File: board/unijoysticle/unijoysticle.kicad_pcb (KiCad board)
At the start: 2 copper layers, 55.6 x 40.6 mm, 13 parts, among them IC1 7405, IC2 7405, J1 DB9_Female, J2 DB9_Female, J3 Barrel_Jack, SW1 SW_Push

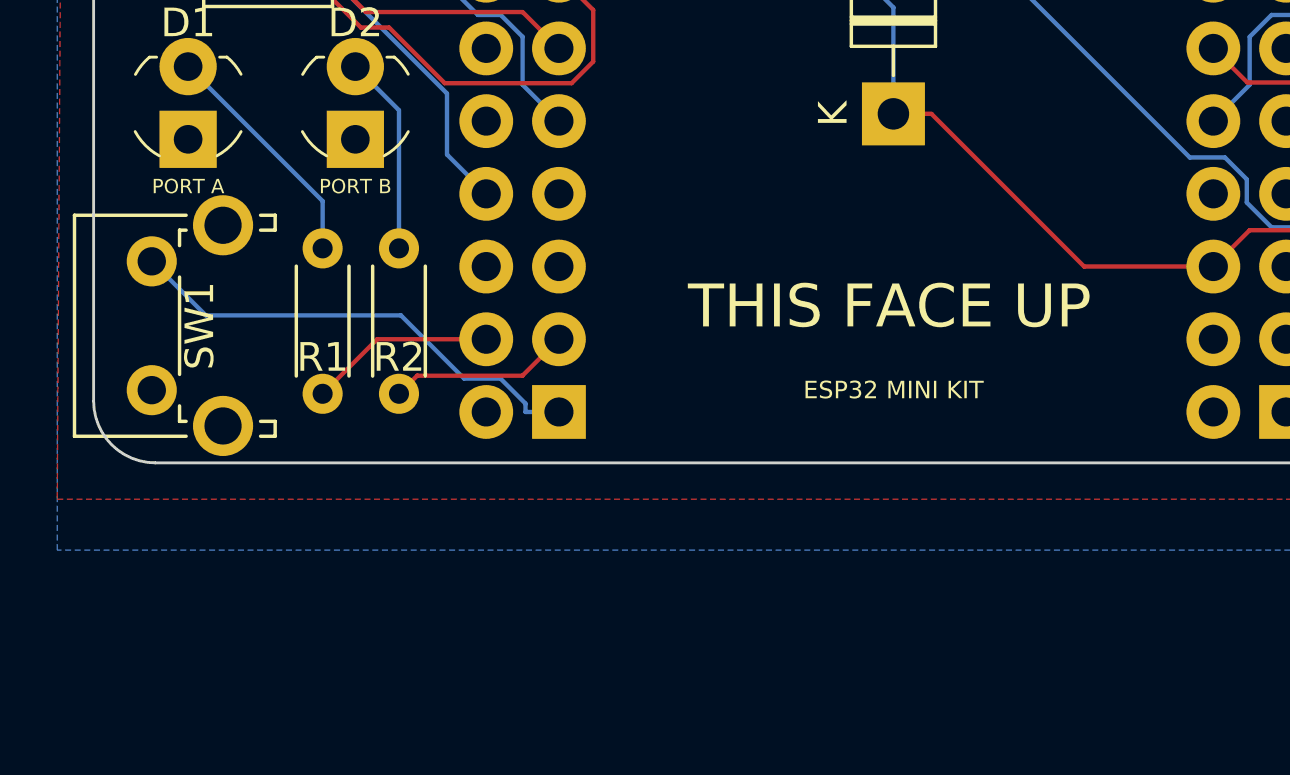
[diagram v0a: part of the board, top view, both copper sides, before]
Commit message: board: renamed 'Parts' -> 'Unijoysticle'
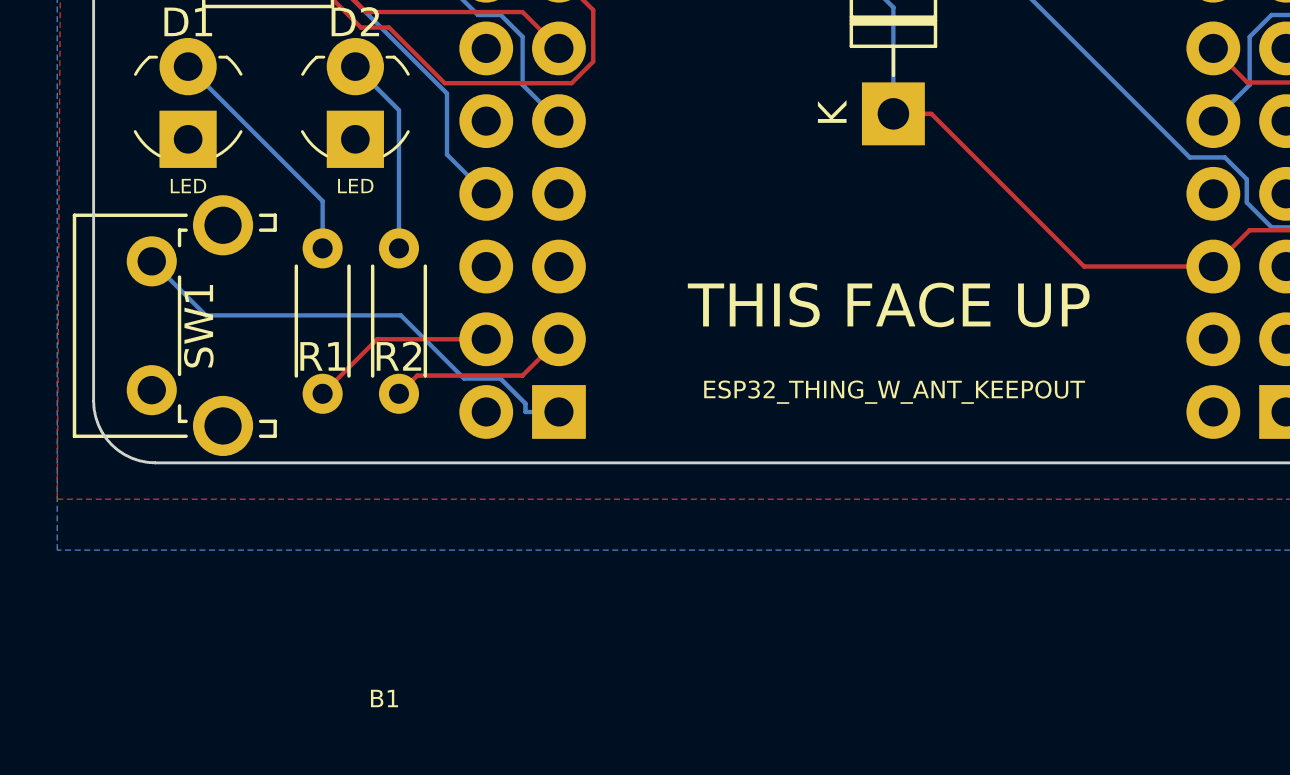
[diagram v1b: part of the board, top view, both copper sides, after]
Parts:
- B1: renamed from ?; value ESP32 MINI KIT -> ESP32_THING_W_ANT_KEEPOUT
- D1: value PORT A -> LED
- D2: value PORT B -> LED
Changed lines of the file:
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@@
-(kicad_pcb (version 20171130) (host pcbnew "(5.0.2-5-10.14)")
+(kicad_pcb (version 20171130) (host pcbnew "(5.1.0-0)")
   (general
     (thickness 1.6002)
@@
     (zone_45_only no)
     (trace_min 0.1524)
-    (segment_width 0.2)
-    (edge_width 0.1)
     (via_size 0.6858)
     (via_drill 0.3302)
@@
     (uvia_min_size 0.2)
     (uvia_min_drill 0.1)
+    (edge_width 0.1)
+    (segment_width 0.2)
     (pcb_text_width 0.3)
     (pcb_text_size 1.5 1.5)
@@
       (effects (font (size 1 1) (thickness 0.15)))
     )
-    (fp_text value "PORT A" (at -4.191 0 180) (layer F.SilkS)
+    (fp_text value LED (at -4.191 0 180) (layer F.SilkS)
       (effects (font (size 0.5 0.5) (thickness 0.1)))
     )
@@
     (descr "MH-ET LIVE MiniKit for ESP32")
     (tags ESP32)
-    (fp_text reference "" (at -2.286 1.143) (layer F.SilkS)
+    (fp_text reference B1 (at -2.286 1.143) (layer F.SilkS)
       (effects (font (size 0.6096 0.6096) (thickness 0.127)))
     )
-    (fp_text value "ESP32 MINI KIT" (at 15.494 -9.652 180) (layer F.SilkS)
+    (fp_text value ESP32_THING_W_ANT_KEEPOUT (at 15.494 -9.652 180) (layer F.SilkS)
       (effects (font (size 0.6096 0.6096) (thickness 0.127)))
     )
@@
       (effects (font (size 1 1) (thickness 0.15)))
     )
-    (fp_text value "PORT B" (at -4.191 0) (layer F.SilkS)
+    (fp_text value LED (at -4.191 0) (layer F.SilkS)
       (effects (font (size 0.5 0.5) (thickness 0.1)))
     )

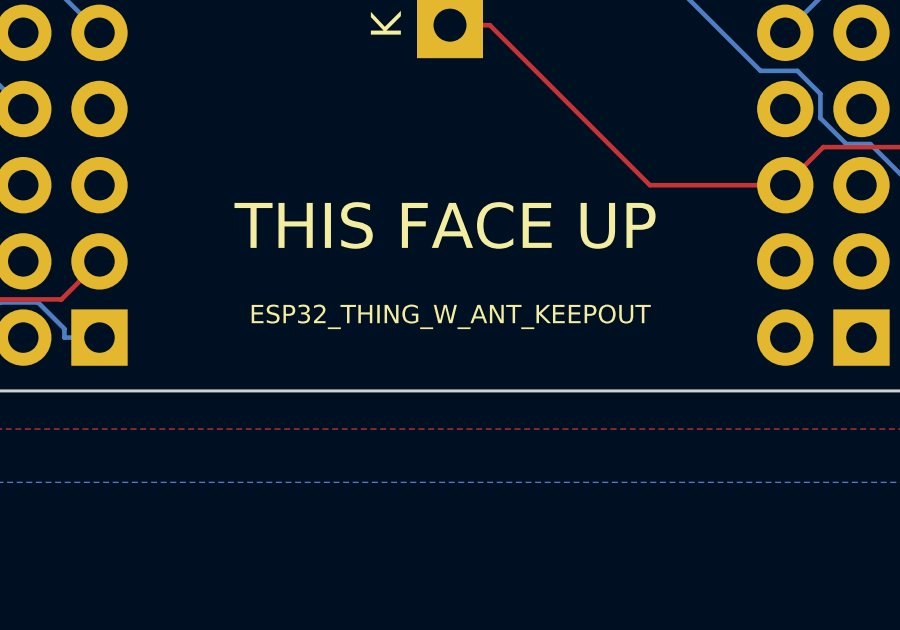
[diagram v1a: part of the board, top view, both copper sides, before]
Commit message: firmware: uni_gpio
schematic: borders around components
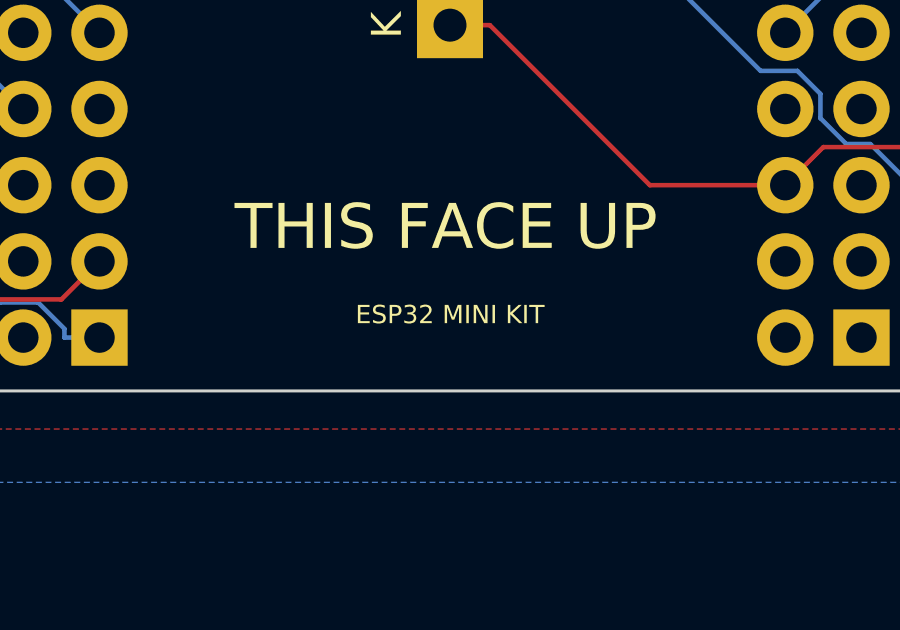
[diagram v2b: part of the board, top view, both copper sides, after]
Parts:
- B1: value ESP32_THING_W_ANT_KEEPOUT -> ESP32 MINI KIT
- R1, R2: value R -> 100
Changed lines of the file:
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@@
   (general
     (thickness 1.6002)
-    (drawings 13)
+    (drawings 12)
     (tracks 169)
     (zones 0)
@@
   )
   (page A4)
+  (title_block
+    (title Unijoysticle)
+    (date 2019-03-13)
+    (rev v0.0.1)
+  )
   (layers
     (0 F.Cu signal)
@@
       (effects (font (size 0.6096 0.6096) (thickness 0.127)))
     )
-    (fp_text value ESP32_THING_W_ANT_KEEPOUT (at 15.494 -9.652 180) (layer F.SilkS)
+    (fp_text value "ESP32 MINI KIT" (at 15.494 -9.652 180) (layer F.SilkS)
       (effects (font (size 0.6096 0.6096) (thickness 0.127)))
     )
@@
       (effects (font (size 1 1) (thickness 0.15)))
     )
-    (fp_text value R (at -1.905 0 180) (layer F.Fab)
+    (fp_text value 100 (at -1.905 0 180) (layer F.Fab)
       (effects (font (size 1 1) (thickness 0.15)))
     )
@@
       (effects (font (size 1 1) (thickness 0.15)))
     )
-    (fp_text value R (at -1.905 0 180) (layer F.Fab)
+    (fp_text value 100 (at -1.905 0 180) (layer F.Fab)
       (effects (font (size 1 1) (thickness 0.15)))
     )
@@
     (effects (font (size 1.5 1.5) (thickness 0.3)) (justify mirror))
   )
-  (dimension 20.955 (width 0.3) (layer Dwgs.User)
-    (gr_text "20.955 mm" (at 142.3035 43.493) (layer Dwgs.User)
-      (effects (font (size 1.5 1.5) (thickness 0.3)))
-    )
-    (feature1 (pts (xy 131.826 79.121) (xy 131.826 45.006579)))
-    (feature2 (pts (xy 152.781 79.121) (xy 152.781 45.006579)))
-    (crossbar (pts (xy 152.781 45.593) (xy 131.826 45.593)))
-    (arrow1a (pts (xy 131.826 45.593) (xy 132.952504 45.006579)))
-    (arrow1b (pts (xy 131.826 45.593) (xy 132.952504 46.179421)))
-    (arrow2a (pts (xy 152.781 45.593) (xy 151.654496 45.006579)))
-    (arrow2b (pts (xy 152.781 45.593) (xy 151.654496 46.179421)))
-  )
   (gr_line (start 116.967 115.57) (end 168.275 115.57) (layer Edge.Cuts) (width 0.1))

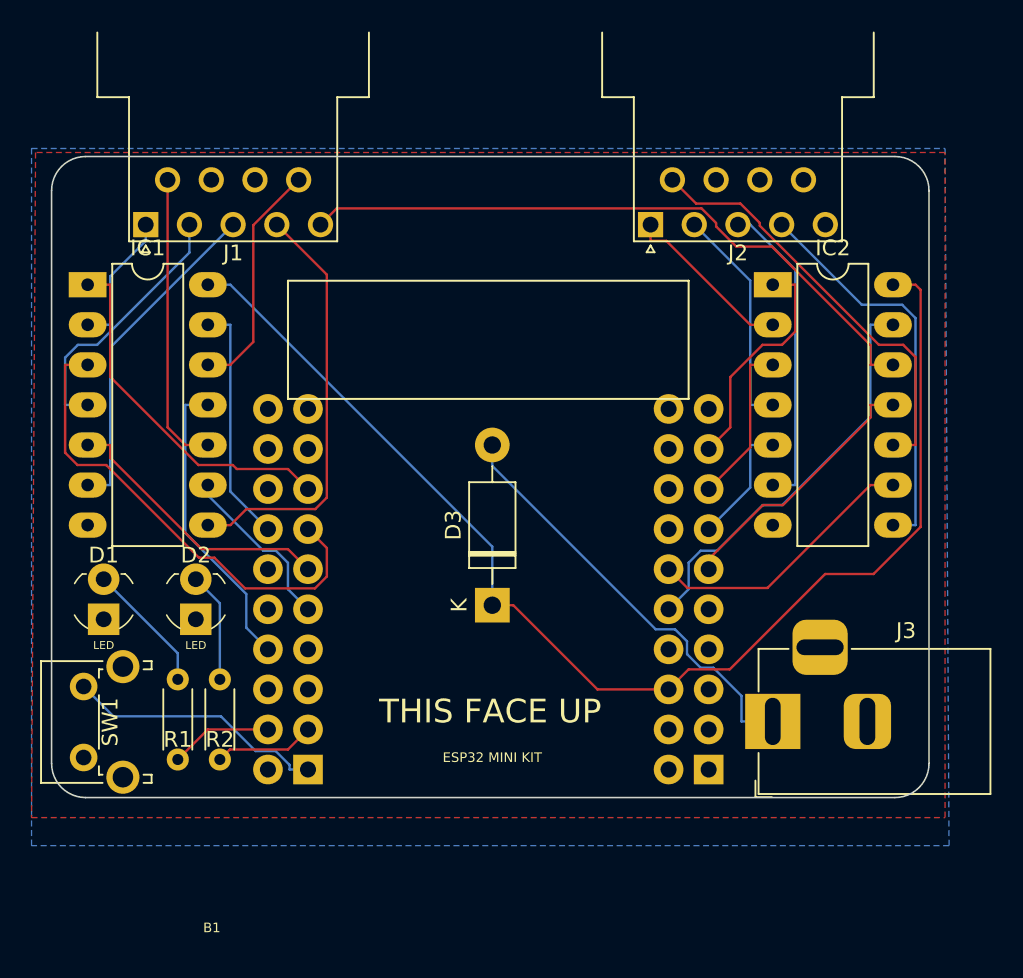
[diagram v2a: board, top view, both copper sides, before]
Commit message: firmware: support for new mappings (v2)
board: board slightly bigger, diode smaller, resistrors larger
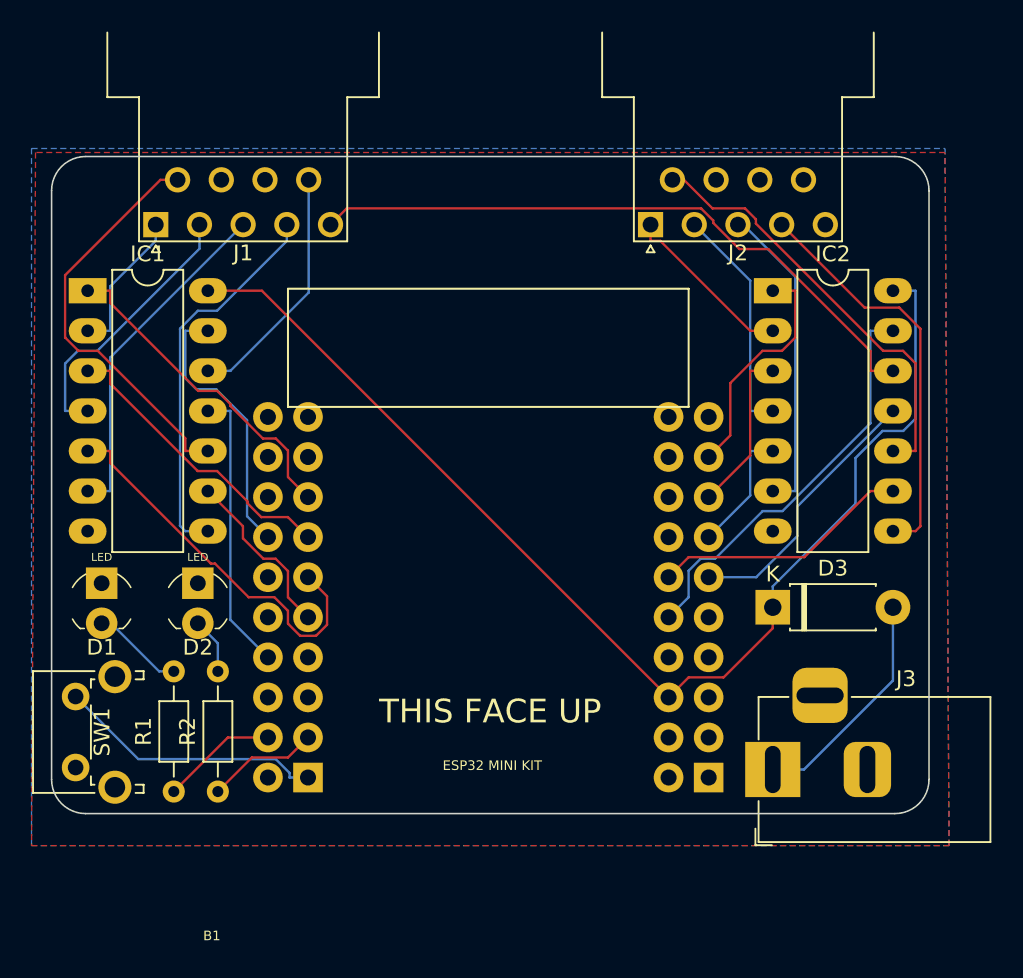
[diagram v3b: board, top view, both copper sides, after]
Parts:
- D3: footprint Diode_THT:D_DO-41_SOD81_P10.16mm_Horizontal -> Diode_THT:D_DO-41_SOD81_P7.62mm_Horizontal
- R1, R2: footprint Resistor_THT:R_Axial_DIN0204_L3.6mm_D1.6mm_P5.08mm_Horizontal -> Resistor_THT:R_Axial_DIN0204_L3.6mm_D1.6mm_P7.62mm_Horizontal
- moved D3 17.8 mm to (160.5, 103.5), turned to 0 degrees
- moved J3 3.05 mm to (160.5, 113.8)
- moved D1 2.80 mm to (118.0, 104.5), turned to 270 degrees
- moved D2 2.80 mm to (124.1, 104.5), turned to 270 degrees
- moved R1 2.05 mm to (122.6, 115.2)
- moved R2 2.04 mm to (125.3, 115.2)
- moved SW1 0.81 mm to (116.3, 113.7)
- moved J1 0.64 mm to (121.4, 79.2)
- moved B1 0.51 mm to (127.3, 123.2)
- moved IC1 0.38 mm to (117.1, 83.4)
- moved IC2 0.38 mm to (160.5, 83.4)
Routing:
- net Net-(D3-Pad2): track 27.2 -> 14.6 mm
- net GPIO_J1DOWN: track 31.0 -> 18.9 mm
- net J1FIRE: track 18.7 -> 26.1 mm
- net GPIO_J1LEFT: track 17.7 -> 24.8 mm
- net VDD: track 79.2 -> 75.6 mm
- net Net-(D2-Pad2): track 6.98 -> 3.57 mm
- net Net-(D1-Pad2): track 8.30 -> 5.83 mm
- net J1RIGHT: track 26.9 -> 24.5 mm
- net GPIO_J1POTX: track 15.4 -> 17.4 mm
- net GPIO_J1UP: track 22.8 -> 20.9 mm
- net GPIO_J1FIRE: track 19.1 -> 18.0 mm
- net GPIO_J2RIGHT: track 17.4 -> 16.5 mm
- net GPIO_J1LED: track 6.50 -> 7.39 mm
- net GPIO_J2LED: track 6.38 -> 7.14 mm
- net J1DOWN: track 16.8 -> 17.5 mm
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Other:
- board size 55.6 x 40.6 mm -> 55.6 x 41.7 mm
- board text added: "Unijoysticle 2 v0.0.2 http://retro.moe"
- board text removed: "Unijoysticle 2 v0.0.1 http://retro.moe"

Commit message: firmware: using GPIOS correctly.
new GPIOS for a some lines so that it doesn't crash
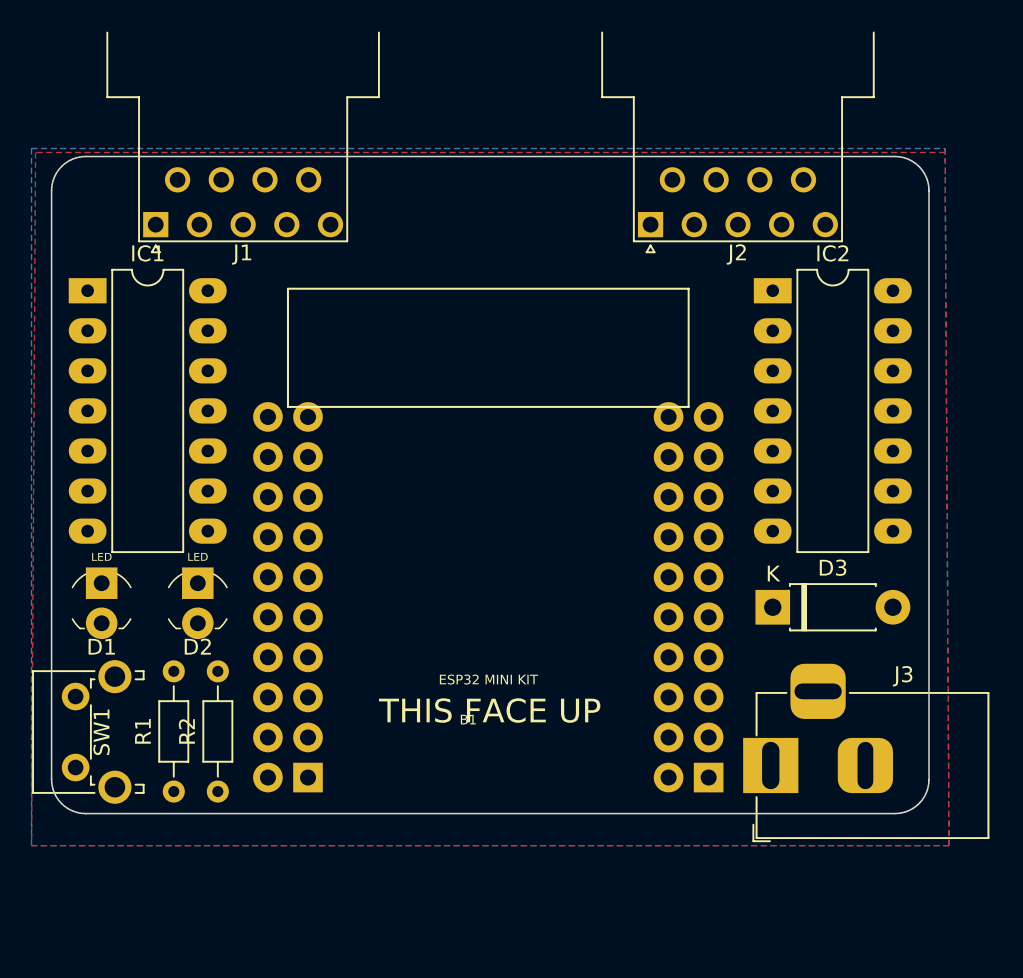
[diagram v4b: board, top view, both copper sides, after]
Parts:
- B1: footprint Parts:MH-ET_LIVE_MINIKIT_ESP32 -> Unijoysticle:MH-ET_LIVE_MINIKIT_ESP32
- J3: footprint Connector_BarrelJack:BarrelJack_Horizontal -> Unijoysticle:BarrelJack_Horizontal
- moved J3 0.28 mm to (160.4, 113.5)
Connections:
- B1 pad 33: Net-(B1-Pad33) -> GPIO_J1POTX
- B1 pad 35: GPIO_J1POTX -> Net-(B1-Pad35)
- B1 pad 5: Net-(B1-Pad5) -> GPIO_J1LED
- B1 pad 9: GPIO_J1LED -> Net-(B1-Pad9)
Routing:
- net VDD: track 75.6 -> 0.00 mm
- net J1POTY: track 41.2 -> 0.00 mm
- net J2FIRE: track 27.4 -> 0.00 mm
- net GPIO_J1POTY: track 26.2 -> 0.00 mm
- net J1FIRE: track 26.1 -> 0.00 mm
- net J2RIGHT: track 25.9 -> 0.00 mm
- net GPIO_J1LEFT: track 24.8 -> 0.00 mm
- net J1RIGHT: track 24.5 -> 0.00 mm
- net J1LEFT: track 21.8 -> 0.00 mm
- net GPIO_J1UP: track 20.9 -> 0.00 mm
- net J2LEFT: track 20.0 -> 0.00 mm
- net GPIO_J1DOWN: track 18.9 -> 0.00 mm
- net GPIO_J1FIRE: track 18.0 -> 0.00 mm
- net J1DOWN: track 17.5 -> 0.00 mm
- net GPIO_J1POTX: track 17.4 -> 0.00 mm
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
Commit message: board: gerber files for PCBWay
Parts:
- added REF**: OSHW-Logo2_7.3x6mm_SilkScreen, Symbol:OSHW-Logo2_7.3x6mm_SilkScreen, F.Cu at (142.6, 86.9)
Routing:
- net VDD: track 0.00 -> 76.6 mm
- net J1POTY: track 0.00 -> 45.6 mm
- net J2RIGHT: track 0.00 -> 27.4 mm
- net J1FIRE: track 0.00 -> 26.1 mm
- net GPIO_J1POTY: track 0.00 -> 26.1 mm
- net J2FIRE: track 0.00 -> 25.5 mm
- net GPIO_J1POTX: track 0.00 -> 25.1 mm
- net J1RIGHT: track 0.00 -> 24.2 mm
- net J1LEFT: track 0.00 -> 21.8 mm
- net GPIO_J1UP: track 0.00 -> 20.9 mm
- net GPIO_J2FIRE: track 0.00 -> 20.7 mm
- net J2LEFT: track 0.00 -> 20.3 mm
- net GPIO_J1FIRE: track 0.00 -> 19.7 mm
- net GPIO_J1DOWN: track 0.00 -> 18.9 mm
- net J1DOWN: track 0.00 -> 17.5 mm
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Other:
- board text added: "Rev B"
- board text added: "Unijoysticle 2 http://retro.moe"
- board text removed: "Unijoysticle 2 v0.0.2 http://retro.moe"
